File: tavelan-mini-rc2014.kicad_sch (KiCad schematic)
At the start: 23 parts, among them J1 Alternate_Reset, J2 Regulated_Power, SW1 Reset

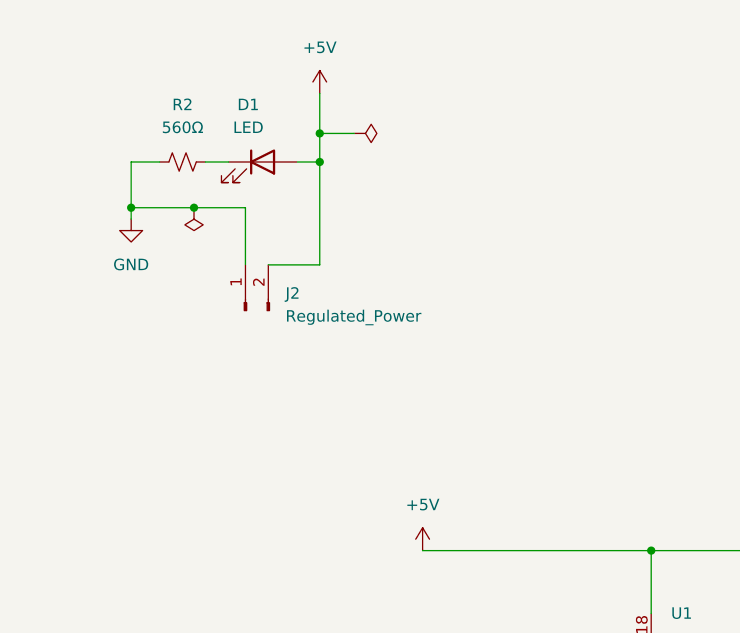
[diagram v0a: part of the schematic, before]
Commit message: Ground pour; add power switch header
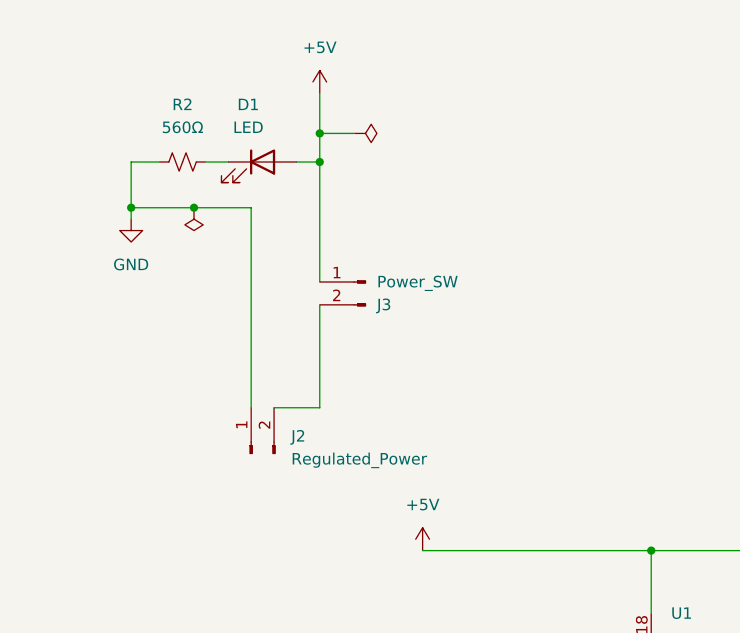
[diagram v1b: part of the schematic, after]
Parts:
- added J3: Power_SW, TerminalBlock_TE-Connectivity:TerminalBlock_TE_282834-2_1x02_P2.54mm_Horizontal, symbol Connector:Conn_01x02_Pin
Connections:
- net +5V: now also J3.1 (Pin_1); no longer J2.2 (Pin_2)
- new net: J2.2 (Pin_2), J3.2 (Pin_2)
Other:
- moved on the sheet: J2
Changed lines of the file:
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@@
 	)
 	(junction
-		(at 48.26 78.74)
+		(at 240.03 205.105)
 		(diameter 0)
 		(color 0 0 0 0)
 	)
 	(junction
-		(at 240.03 205.105)
+		(at 48.26 78.74)
 		(diameter 0)
 		(color 0 0 0 0)
@@
 	(wire
 		(pts
-			(xy 48.26 90.17) (xy 48.26 78.74)
-		)
-		(stroke
-			(width 0)
-			(type default)
-		)
-	)
-	(wire
-		(pts
 			(xy 30.48 78.74) (xy 27.305 78.74)
 		)
@@
 	(wire
 		(pts
-			(xy 42.545 90.17) (xy 48.26 90.17)
+			(xy 43.18 106.045) (xy 48.26 106.045)
 		)
 		(stroke
@@
 	(wire
 		(pts
-			(xy 40.005 90.17) (xy 40.005 83.82)
+			(xy 40.64 106.045) (xy 40.64 83.82)
 		)
 		(stroke
@@
 	(wire
 		(pts
+			(xy 48.26 78.74) (xy 48.26 92.075)
+		)
+		(stroke
+			(width 0)
+			(type default)
+		)
+	)
+	(wire
+		(pts
 			(xy 38.735 38.735) (xy 44.45 38.735)
 		)
@@
 	(wire
 		(pts
-			(xy 40.005 83.82) (xy 34.29 83.82)
+			(xy 40.64 83.82) (xy 34.29 83.82)
 		)
 		(stroke
@@
 	(wire
 		(pts
+			(xy 48.26 94.615) (xy 48.26 106.045)
+		)
+		(stroke
+			(width 0)
+			(type default)
+		)
+	)
+	(wire
+		(pts
 			(xy 34.29 83.82) (xy 27.305 83.82)
 		)
@@
 	)
 	(symbol
+		(lib_id "Connector:Conn_01x02_Pin")
+		(at 53.34 92.075 0)
+		(mirror y)
+		(unit 1)
+		(exclude_from_sim no)
+		(in_bom yes)
+		(on_board yes)
+		(dnp no)
+		(property "Reference" "J3"
+			(at 54.61 94.6151 0)
+			(effects
+				(font
+					(size 1.27 1.27)
+				)
+				(justify right)
+			)
+		)
+		(property "Value" "Power_SW"
+			(at 54.61 92.0751 0)
+			(effects
+				(font
+					(size 1.27 1.27)
+				)
+				(justify right)
+			)
+		)
+		(property "Footprint" "TerminalBlock_TE-Connectivity:TerminalBlock_TE_282834-2_1x02_P2.54mm_Horizontal"
+			(at 53.34 92.075 0)
+			(effects
+				(font
+					(size 1.27 1.27)
+				)
+				(hide yes)
+			)
+		)
+		(property "Datasheet" "~"
+			(at 53.34 92.075 0)
+			(effects
+				(font
+					(size 1.27 1.27)
+				)
+				(hide yes)
+			)
+		)
+		(property "Description" ""
+			(at 53.34 92.075 0)
+			(effects
+				(font
+					(size 1.27 1.27)
+				)
+				(hide yes)
+			)
+		)
+		(pin "2"
+		)
+		(pin "1"
+		)
+		(instances
+			(project "tavelan-mini-rc2014"
+				(path "/7425670c-d60a-42da-8c57-0373ad05bc43"
+					(reference "J3")
+					(unit 1)
+				)
+			)
+		)
+	)
+	(symbol
 		(lib_id "power:+5V")
 		(at 123.19 86.36 0)
@@
 	(symbol
 		(lib_id "Connector:Conn_01x02_Pin")
-		(at 40.005 95.25 90)
+		(at 40.64 111.125 90)
 		(unit 1)
 		(exclude_from_sim no)
@@
 		(fields_autoplaced yes)
 		(property "Reference" "J2"
-			(at 44.45 93.345 90)
+			(at 45.085 109.22 90)
 			(effects
 				(font
@@
 		)
 		(property "Value" "Regulated_Power"
-			(at 44.45 95.885 90)
+			(at 45.085 111.76 90)
 			(effects
 				(font
@@
 		)
 		(property "Footprint" "TerminalBlock_TE-Connectivity:TerminalBlock_TE_282834-2_1x02_P2.54mm_Horizontal"
-			(at 40.005 95.25 0)
+			(at 40.64 111.125 0)
 			(effects
 				(font
@@
 		)
 		(property "Datasheet" "~"
-			(at 40.005 95.25 0)
+			(at 40.64 111.125 0)
 			(effects
 				(font
@@
 		)
 		(property "Description" ""
-			(at 40.005 95.25 0)
+			(at 40.64 111.125 0)
 			(effects
 				(font
